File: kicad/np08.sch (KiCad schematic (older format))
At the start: 27 parts, among them J1 SENS_D1, J10 SRV2, J11 SRV1, J2 SENS_D2, J3 SENS_D3, J4 SRV6, J5 USB-78L05, J6 SRV5, J7 SRV4, J8 USB-LM7805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

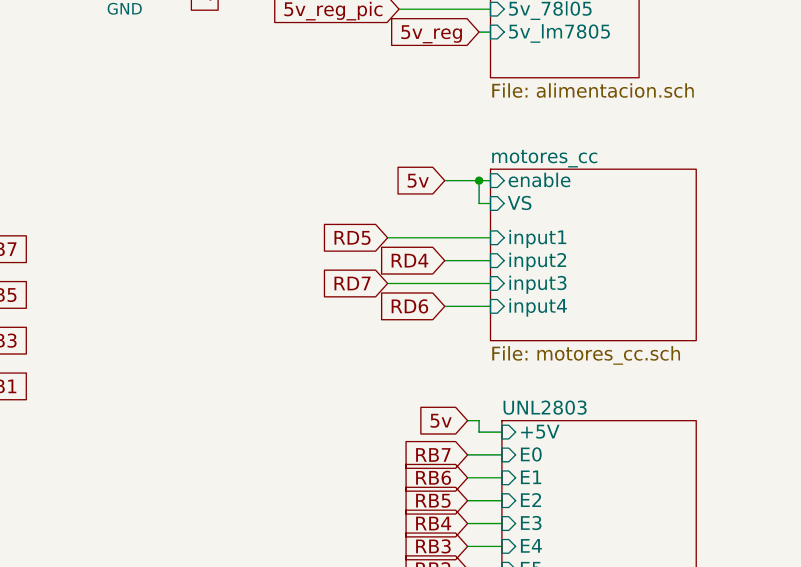
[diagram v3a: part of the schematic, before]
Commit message: cambios para el desarrollo de la placa np08, ahora usa 6 pines para servos y 3 pines para dig
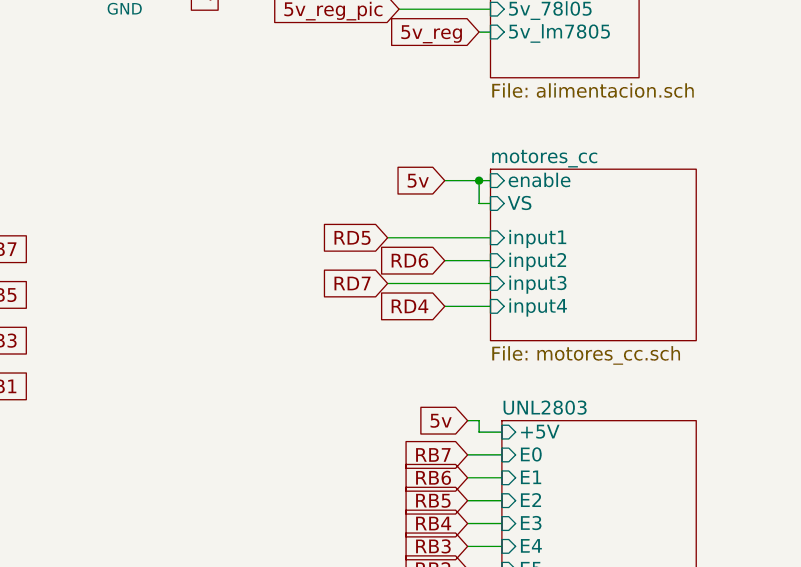
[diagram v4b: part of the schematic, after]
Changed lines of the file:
@@
 Wire Wire Line
 	7700 4500 7550 4500
-Text GLabel 10000 2450 0    60   Input ~ 0
+Text GLabel 10000 2650 0    60   Input ~ 0
 RD4
 Text GLabel 9750 2350 0    60   Input ~ 0
 RD5
-Text GLabel 10000 2650 0    60   Input ~ 0
+Text GLabel 10000 2450 0    60   Input ~ 0
 RD6
 Text GLabel 9750 2550 0    60   Input ~ 0
